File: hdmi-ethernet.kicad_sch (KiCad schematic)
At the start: 46 parts

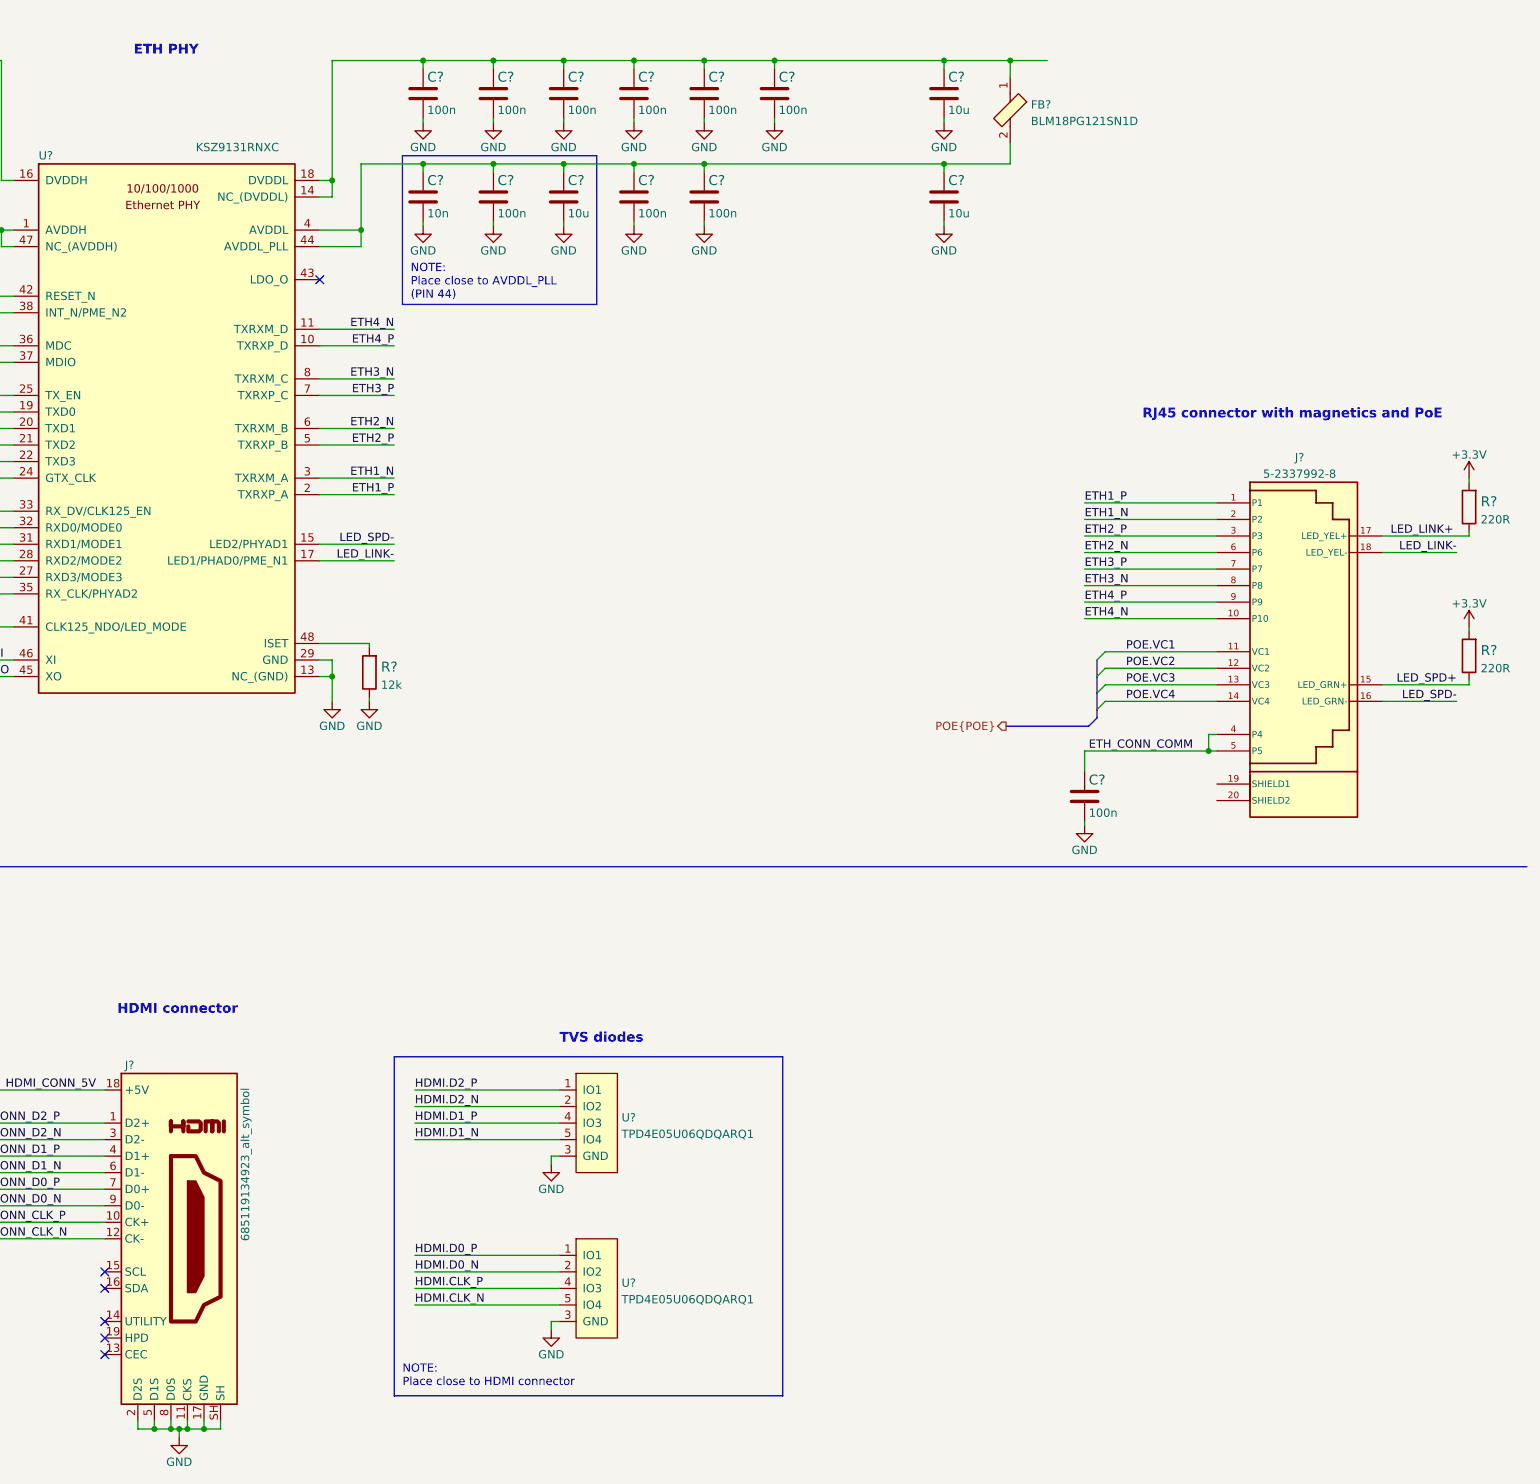
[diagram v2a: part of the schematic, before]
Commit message: Unify reference designator placement
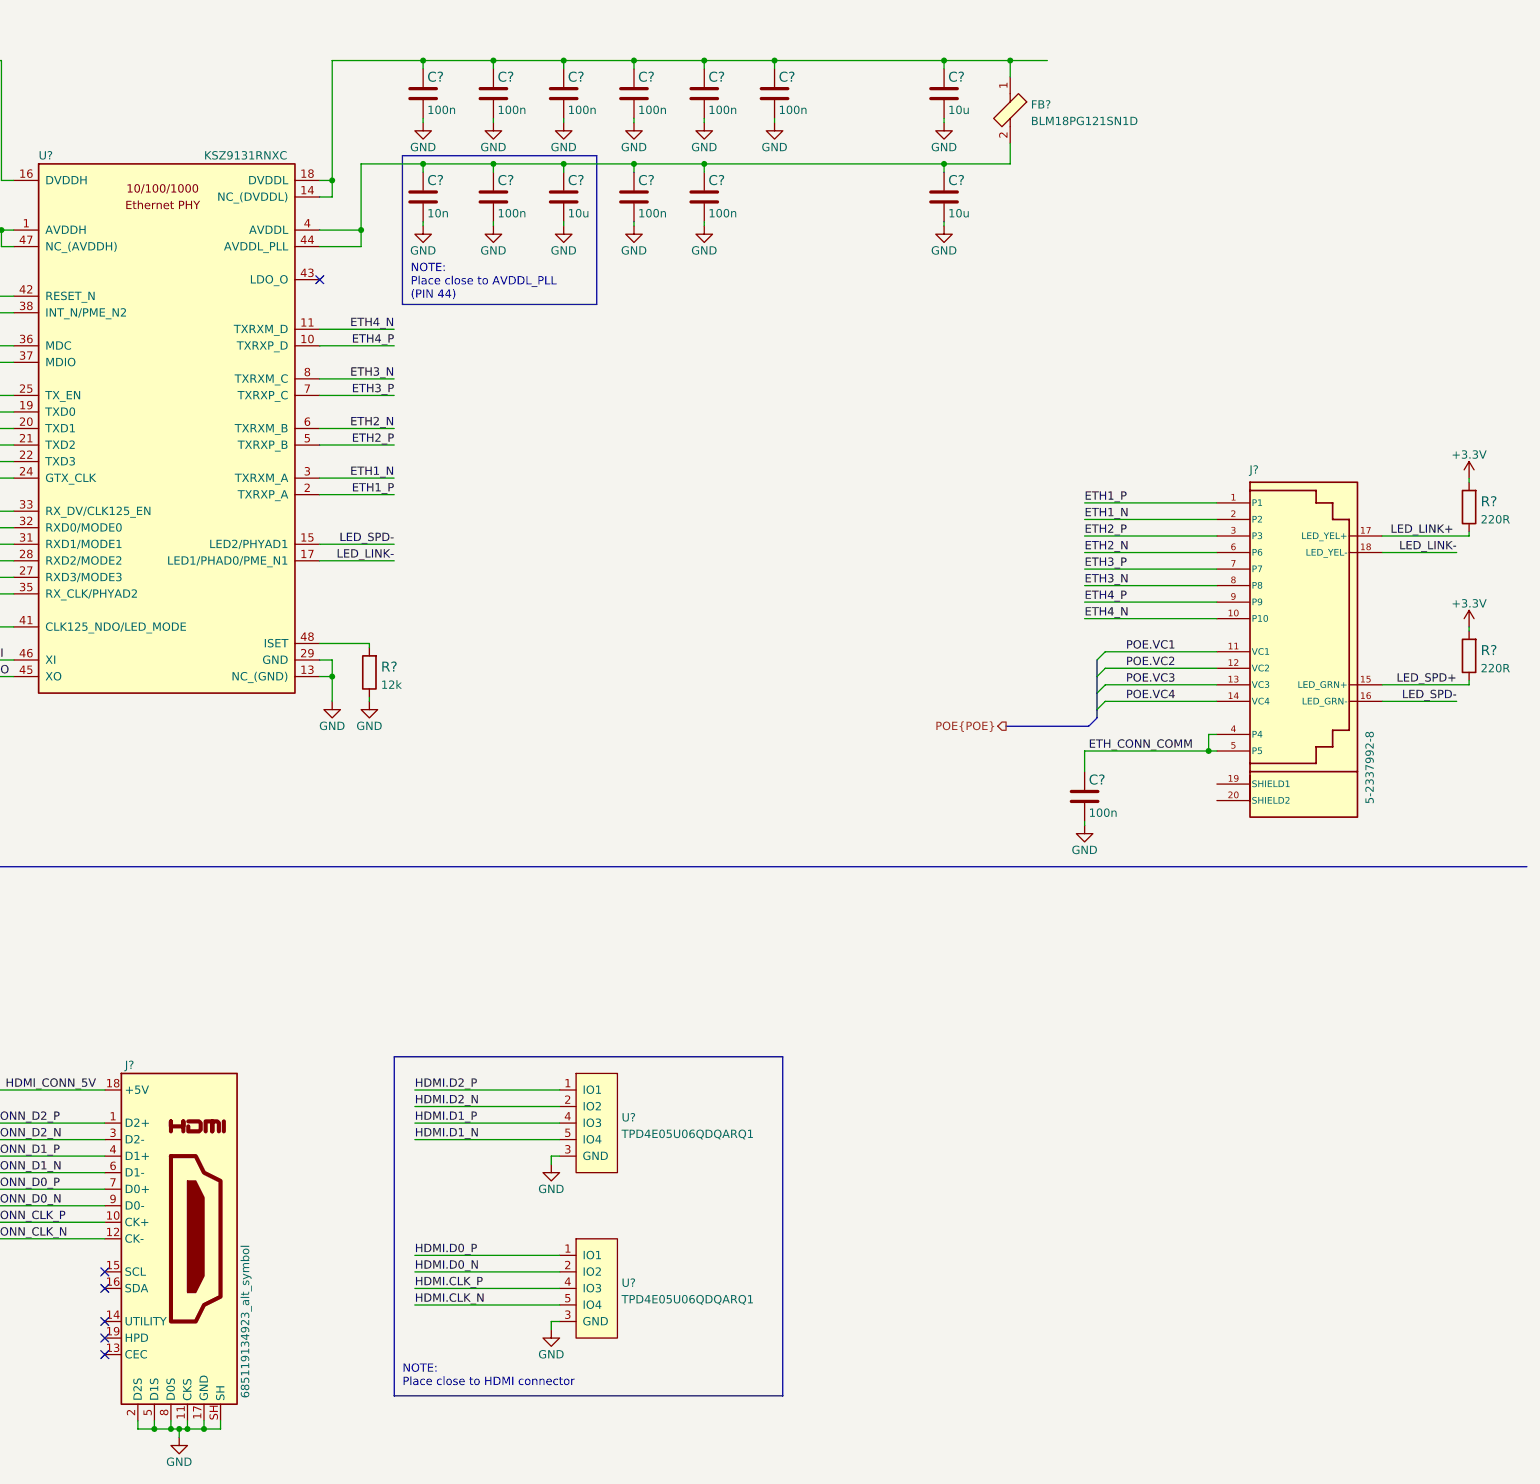
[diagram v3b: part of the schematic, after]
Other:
- note removed: "ETH PHY"
- note removed: "HDMI connector"
- note removed: "RJ45 connector with magnetics and PoE"
- note removed: "TVS diodes"
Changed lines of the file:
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@@
     (effects (font (size 1.27 1.27)) (justify left bottom))
-  )
-  (text "RJ45 connector with magnetics and PoE " (at 347.345 77.47 0)
-    (effects (font (size 1.5 1.5) (thickness 0.4) bold) (justify left bottom))
   )
   (text "NOTE:\nPlace close to AVDDL_PLL\n(PIN 44)" (at 234.95 59.055 0)
@@
   (text "NOTE:\nPlace close to HDMI connector" (at 233.68 226.06 0)
     (effects (font (size 1.27 1.27)) (justify left bottom))
-  )
-  (text "ETH PHY" (at 192.405 21.59 0)
-    (effects (font (size 1.5 1.5) (thickness 0.4) bold) (justify left bottom))
   )
   (text "HDMI" (at 15.24 151.765 0)
     (effects (font (size 2 2) (thickness 0.4) bold) (justify left bottom))
   )
-  (text "HDMI connector" (at 189.865 168.91 0)
-    (effects (font (size 1.5 1.5) (thickness 0.4) bold) (justify left bottom))
-  )
   (text "Ethernet" (at 14.605 18.415 0)
     (effects (font (size 2 2) (thickness 0.4) bold) (justify left bottom))
   )
-  (text "TVS diodes" (at 257.81 173.355 0)
-    (effects (font (size 1.5 1.5) (thickness 0.4) bold) (justify left bottom))
-  )
   (label "ETH4_P" (at 338.455 105.41 0)
     (effects (font (size 1.27 1.27)) (justify left bottom))
@@
   (symbol (lib_id "antmicroModularConnectorsJacksWithMagnetics:5-2337992-8") (at 371.475 110.49 0) (unit 1)
     (in_bom yes) (on_board yes)
-    (property "Reference" "J?" (id 0) (at 371.475 83.1881 0))
-    (property "Value" "5-2337992-8" (id 1) (at 371.475 85.725 0))
+    (property "Reference" "J?" (id 0) (at 364.49 85.09 0))
+    (property "Value" "5-2337992-8" (id 1) (at 382.27 130.81 90))
     (property "Footprint" "antmicro-footprints:5-2337992-8" (id 2) (at 373.38 146.05 0)
       (effects (font (size 1.27 1.27)) hide)
@@
     (in_bom yes) (on_board yes)
     (property "Reference" "J?" (id 0) (at 191.77 176.53 0))
-    (property "Value" "685119134923_alt_symbol" (id 1) (at 209.55 191.77 90))
+    (property "Value" "685119134923_alt_symbol" (id 1) (at 209.55 215.9 90))
     (property "Footprint" "antmicro-footprints:HDMI_A_Female_685119134923" (id 2) (at 168.91 248.92 0)
       (effects (font (size 1.27 1.27)) (justify left) hide)
@@
   )
   (symbol (lib_id "antmicroInterfaceControllers:KSZ9131RNXC") (at 177.8 38.1 0) (unit 1)
-    (in_bom yes) (on_board yes) (fields_autoplaced)
+    (in_bom yes) (on_board yes)
     (property "Reference" "U?" (id 0) (at 177.8 36.83 0)
       (effects (font (size 1.27 1.27)) (justify left))
     )
-    (property "Value" "KSZ9131RNXC" (id 1) (at 201.93 35.56 0)
-      (effects (font (size 1.27 1.27)) (justify left))
-    )
+    (property "Value" "KSZ9131RNXC" (id 1) (at 203.2 36.83 0)
+      (effects (font (size 1.27 1.27)) (justify left))
+    )

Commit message: Add bootstrap resistors to ETH PHY IC
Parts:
- added C?: C_100n_0201, antmicro-footprints:0201-res, symbol antmicroCapacitorsmisc:C_100n_0201
- added R? (x10): R_2k2_0402, antmicro-footprints:0402-res, symbol antmicroResistors0402:R_2k2_0402
- added R? (x11): R_10k_0402, antmicro-footprints:0402-res, symbol antmicroResistors0402:R_10k_0402
- added R?: R_1k_0402, antmicro-footprints:0402-res, symbol antmicroResistors0402:R_1k_0402
- added R?: R_10R_0603, antmicro-footprints:0603-res, symbol antmicroResistors0603:R_10R_0603
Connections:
- net ETH_RGMII.GTR_CLK: now also R?.1, R?.1
- net ETH_RGMII.MDIO: now also R?.2
- net ETH_RGMII.RXD0: now also R?.1, R?.1
- net ETH_RGMII.RXD1: now also R?.1, R?.1
- net ETH_RGMII.RXD2: now also R?.1, R?.1
- net ETH_RGMII.RXD3: now also R?.1, R?.1
- net ETH_RGMII.RX_DV: now also R?.1, R?.1
- net ETH_RGMII.~{INT}: now also R?.1, R?.1
- net ETH_RGMII.~{RESET}: now also R?.2
- net GND: now also C?.2, R?.1, R?.2, R?.2, R?.2, R?.2, R?.2, R?.2, R?.2, R?.2, R?.2, R?.2
- net LED_LINK-: now also R?.1, R?.1
- net LED_SPD-: now also R?.1, R?.1
- net at J?.19 (SHIELD1): now also J?.20 (SHIELD2), C?.1, R?.2
- net ETH_RGMII.CLK125 renamed ETH_RGMII.REFCLK
- net ETH_RGMII.REFCLK: now also R?.1, R?.1
- new net: R?.1, R?.1
- new net: R?.2, R?.2, R?.2, R?.2, R?.2, R?.2, R?.2, R?.2, R?.2, R?.2
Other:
- note added: "ALLPHYAD"
- note added: "Bootstrap configuration"
- note added: "CLK125_EN"
- note added: "LED_MODE"
- note added: "MODE0"
- note added: "MODE1"
- note added: "MODE2"
- note added: "MODE3"
- note added: "PHYAD0"
- note added: "PHYAD1"
- note added: "PHYAD2"
- note added: "Pull down"
- note added: "Pull up"
- note added: "default: MODE[3:0] : 1100 (see datasheet table 3-8) PHYAD[4:0]: 00011 CLK125_EN: NO LED_MODE: Individual-LED ALLPHYAD: NO"
- moved on the sheet: C?, FB?, J?, R?

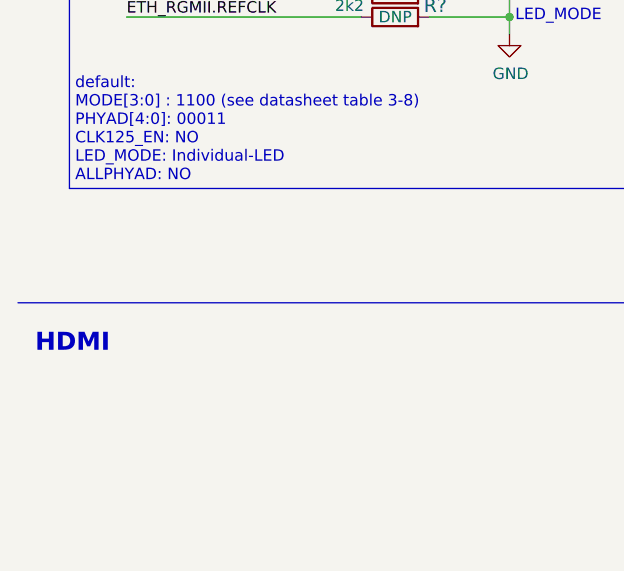
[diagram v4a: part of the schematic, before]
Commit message: Add todo to HDMI
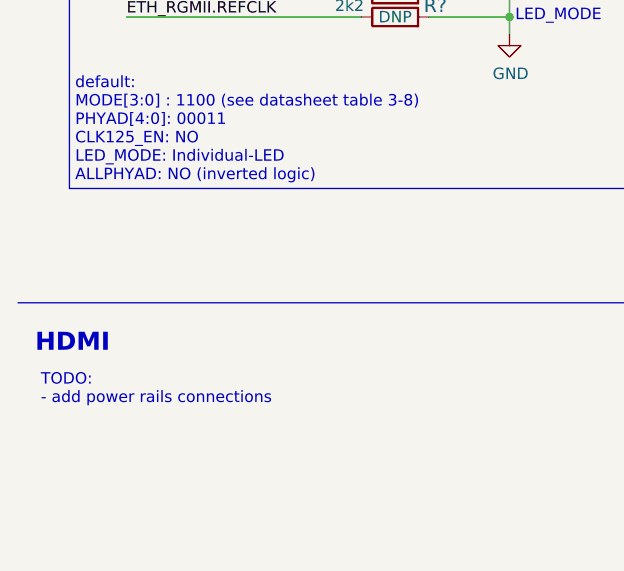
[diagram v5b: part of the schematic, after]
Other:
- note added: "default: MODE[3:0] : 1100 (see datasheet table 3-8) PHYAD[4:0]: 00011 CLK125_EN: NO LED_MODE: Individual-LED ALLPHYAD: NO (inverted logic)"
- note removed: "default: MODE[3:0] : 1100 (see datasheet table 3-8) PHYAD[4:0]: 00011 CLK125_EN: NO LED_MODE: Individual-LED ALLPHYAD: NO"
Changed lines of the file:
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@@
+    (effects (font (size 1.27 1.27)) (justify left bottom))
+  )
+  (text "TODO:\n- add power rails connections" (at 15.875 157.48 0)
     (effects (font (size 1.27 1.27)) (justify left bottom))
   )
@@
     (effects (font (size 1.27 1.27)) (justify left bottom))
   )
-  (text "default:\nMODE[3:0] : 1100 (see datasheet table 3-8)\nPHYAD[4:0]: 00011 \nCLK125_EN: NO\nLED_MODE: Individual-LED\nALLPHYAD: NO"
+  (text "default:\nMODE[3:0] : 1100 (see datasheet table 3-8)\nPHYAD[4:0]: 00011 \nCLK125_EN: NO\nLED_MODE: Individual-LED\nALLPHYAD: NO (inverted logic)"
     (at 19.685 132.715 0)
     (effects (font (size 1.27 1.27)) (justify left bottom))

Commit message: Add RMII ETH PHY
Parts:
- added C? (x4): C_10p_0402, antmicro-footprints:0402-cap, symbol antmicroCapacitors0402:C_10p_0402
- added C? (x3): C_10u_0402, antmicro-footprints:0402-cap, symbol antmicroCapacitors0402:C_10u_0402
- added C? (x9): C_100n_0201, antmicro-footprints:0201-res, symbol antmicroCapacitorsmisc:C_100n_0201
- added C? (x2): C_22p_0402, antmicro-footprints:0402-cap, symbol antmicroCapacitors0402:C_22p_0402
- added FB?: BLM18PG121SN1D, antmicro-footprints:0603-res, symbol antmicroFerriteBeadsandChips:BLM18PG121SN1D
- added J?: 5-2337992-8, antmicro-footprints:5-2337992-8, symbol antmicroModularConnectorsJacksWithMagnetics:5-2337992-8
- added R? (x7): R_10k_0402, antmicro-footprints:0402-res, symbol antmicroResistors0402:R_10k_0402
- added R? (x6): R_2k2_0402, antmicro-footprints:0402-res, symbol antmicroResistors0402:R_2k2_0402
- added R? (x8): R_10R_1%_0402, antmicro-footprints:0402-res, symbol antmicroResistors0402:R_10R_1%_0402
- added R? (x4): R_49R9_0402, antmicro-footprints:0402-res, symbol antmicroResistors0402:R_49R9_0402
- added R?: R_10R_0603, antmicro-footprints:0603-res, symbol antmicroResistors0603:R_10R_0603
- added R? (x2): R_220R_0603, antmicro-footprints:0603-res, symbol antmicroResistors0603:R_220R_0603
- added R?: R_1k_0402, antmicro-footprints:0402-res, symbol antmicroResistors0402:R_1k_0402
- added R?: R_1M0_0402, antmicro-footprints:0402-res, symbol antmicroResistors0402:R_1M0_0402
- added R?: R_12k_0402, antmicro-footprints:0402-res, symbol antmicroResistors0402:R_12k_0402
- added U?: LAN8720A-CP-TR-ABC, antmicro-footprints:QFN-24-1EP_4x4mm_P0.5mm_EP2.6x2.6mm, symbol antmicroInterfaceControllers:LAN8720A-CP-TR-ABC
- added Y?: ABM8G-25.000MHZ-18-D2Y-T, antmicro-footprints:KX-7, symbol antmicroCrystals:ABM8G-25.000MHZ-18-D2Y-T
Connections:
- net +3V3: now also R?.2, R?.2
- net ETH1_N: now also C?.1, J?.2 (P2), R?.1, U?.20 (TXN); no longer J?.2 (P2), U?.3 (TXRXM_A)
- net ETH1_P: now also C?.1, J?.1 (P1), R?.1, U?.21 (TXP); no longer J?.1 (P1), U?.2 (TXRXP_A)
- net ETH2_N: now also C?.1, J?.6 (P6), R?.1, U?.22 (RXN); no longer J?.6 (P6), U?.6 (TXRXM_B)
- net ETH2_P: now also C?.1, J?.3 (P3), R?.1, U?.23 (RXP); no longer J?.3 (P3), U?.5 (TXRXP_B)
- net ETH_CONN_COMM: now also C?.1, C?.1, J?.4 (P4), J?.5 (P5); no longer C?.1, J?.4 (P4), J?.5 (P5)
- net ETH_XI: now also C?.1, R?.2, U?.5 (XTAL1/CLKIN), Y?.1; no longer C?.1, R?.2, U?.46 (XI), Y?.1
- net ETH_XO: now also C?.1, R?.1, U?.4 (XTAL2), Y?.3; no longer C?.1, R?.1, U?.45 (XO), Y?.3
- net GND: now also C?.2, C?.2, C?.2, C?.2, C?.2, C?.2, C?.2, C?.2, C?.2, C?.2, C?.2, C?.2, C?.2, C?.2, C?.2, C?.2, C?.2, C?.2, R?.1, R?.1, R?.2, R?.2, R?.2, R?.2, R?.2, R?.2, U?.25 (VSS), Y?.2, Y?.4
- net POE.VC1: now also J?.11 (VC1)
- net POE.VC2: now also J?.12 (VC2)
- net POE.VC3: now also J?.13 (VC3)
- net POE.VC4: now also J?.14 (VC4)
- net GBE_CONN_SH: now reaches C?.1, J?.19 (SHIELD1), J?.20 (SHIELD2), R?.2
- net ETH3_N renamed GBE3_N
- net ETH3_P renamed GBE3_P
- net ETH4_N renamed GBE4_N
- net ETH4_P renamed GBE4_P
- net ETH_RGMII.GTR_CLK renamed GBE_RGMII.GTR_CLK
- net ETH_RGMII.GTX_CLK renamed GBE_RGMII.GTX_CLK
- net ETH_RGMII.MDC renamed GBE_RGMII.MDC
- net ETH_RGMII.MDIO renamed GBE_RGMII.MDIO
- net ETH_RGMII.REFCLK renamed GBE_RGMII.REFCLK
- net ETH_RGMII.RXD0 renamed GBE_RGMII.RXD0
- net ETH_RGMII.RXD1 renamed GBE_RGMII.RXD1
- net ETH_RGMII.RXD2 renamed GBE_RGMII.RXD2
- net ETH_RGMII.RXD3 renamed GBE_RGMII.RXD3
- net ETH_RGMII.RX_DV renamed GBE_RGMII.RX_DV
- net ETH_RGMII.TXD0 renamed GBE_RGMII.TXD0
- net ETH_RGMII.TXD1 renamed GBE_RGMII.TXD1
- net ETH_RGMII.TXD2 renamed GBE_RGMII.TXD2
- net ETH_RGMII.TXD3 renamed GBE_RGMII.TXD3
- net ETH_RGMII.TX_EN renamed GBE_RGMII.TX_EN
- net ETH_RGMII.~{INT} renamed GBE_RGMII.~{INT}
- net ETH_RGMII.~{RESET} renamed GBE_RGMII.~{RESET}
- net LED_LINK+ renamed GBE_LED_LINK+
- net LED_LINK- renamed GBE_LED_LINK-
- net LED_SPD+ renamed GBE_LED_SPD+
- net LED_SPD- renamed GBE_LED_SPD-
- new net: R?.2, R?.2, R?.2, R?.2, R?.2, R?.2
- new net: R?.2, U?.24 (RBIAS)
- new net: C?.1, C?.1, U?.9 (VDDIO)
- new net: R?.1, R?.1
- new net ETH_3V3: C?.1, C?.1, C?.1, C?.1, FB?.1, R?.2, R?.2, R?.2, R?.2, U?.1 (VDD2A), U?.19 (VDD1A)
- new net ETH_CONN_SH: C?.1, J?.19 (SHIELD1), J?.20 (SHIELD2), R?.2
- new net ETH_LED_LINK+: J?.17 (LED_YEL+), R?.1
- new net ETH_LED_LINK-: J?.18 (LED_YEL-), R?.1, R?.1, U?.3 (LED1/REGOFF)
- new net ETH_LED_SPD+: J?.15 (LED_GRN+), R?.1
- new net ETH_LED_SPD-: J?.16 (LED_GRN-), R?.1, R?.1, U?.2 (LED2/nINTSEL)
- new net ETH_PHY_REFCLK: R?.2, U?.14 (INT/REFCLKO)
- new net ETH_PHY_RXD1: R?.1, R?.1, R?.2, U?.7 (RXD1/MODE1)
- new net ETH_PHY_RXDO: R?.1, R?.1, R?.2, U?.8 (RXD0/MODE0)
- new net ETH_PHY_RXER: R?.1, R?.1, R?.2, U?.10 (RXER/PHYAD0)
- new net ETH_PHY_RX_DV: R?.1, R?.1, R?.2, U?.11 (CRS_DV/MODE2)
- new net ETH_PHY_TXD1: R?.2, U?.18 (TXD1)
- new net ETH_PHY_TXDO: R?.2, U?.17 (TXD0)
- new net ETH_PHY_TXEN: R?.2, U?.16 (TXEN)
- new net ETH_RMII.MDC: U?.13 (MDC)
- new net ETH_RMII.MDIO: R?.2, U?.12 (MDIO)
- new net ETH_RMII.REFCLK: R?.1
- new net ETH_RMII.RXD0: R?.1
- new net ETH_RMII.RXD1: R?.1
- new net ETH_RMII.RXER: R?.1
- new net ETH_RMII.RX_DV: R?.1
- new net ETH_RMII.TXD0: R?.1
- new net ETH_RMII.TXD1: R?.1
- new net ETH_RMII.TXEN: R?.1
- new net ETH_RMII.~{RESET}: R?.2, U?.15 (RST)
- new net ETH_VDDCR: C?.1, C?.1, U?.6 (VDDCR)
- new net GBE1_N: J?.2 (P2), U?.3 (TXRXM_A)
- new net GBE1_P: J?.1 (P1), U?.2 (TXRXP_A)
- new net GBE2_N: J?.6 (P6), U?.6 (TXRXM_B)
- new net GBE2_P: J?.3 (P3), U?.5 (TXRXP_B)
- new net GBE_CONN_COMM: C?.1, C?.1, J?.4 (P4), J?.5 (P5)
- new net GBE_XI: C?.1, R?.2, U?.46 (XI), Y?.1
- new net GBE_XO: C?.1, R?.1, U?.45 (XO), Y?.3
- no-connect marks 6 -> 10
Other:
- note added: "Gigabit Ethernet"
- note added: "NOTE: Place close ETH connector"
- note added: "NOTE: Place close to FPGA"
- note added: "NOTE: Place close to PHY IC"
- note added: "REGOFF"
- note added: "default: MODE[2:0] : 111 (see datasheet table 3-4) PHYAD[0]: 0 REGOFF: 0, INT 1.2 V Reg enabled ~{INTSEL}: 0, REF_CLK Out mode"
- note added: "~{INTSEL}"
- moved on the sheet: C?, D?, FB?, J?, R?, U?, Y?
